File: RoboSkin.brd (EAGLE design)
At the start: 20 x 25.4 mm, 9 parts, among them U1 LSM6DS3, U2 VL53L1X

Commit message: New Circuit
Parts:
- removed L1: RES-07859, SparkFun-Passives:0603
- U1: value LSM6DS3 -> LSM6DS3DOT_INDICATION
- moved U2 66.3 mm to (67.3, 29.2)
- moved R4 57.1 mm to (58.4, 47.0)
- moved R5 57.1 mm to (54.6, 47.0)
- moved SV1 53.9 mm to (53.3, 41.9)
- moved C3 49.3 mm to (50.8, 48.3)
- moved C4 49.3 mm to (47.0, 48.3)
- moved R2 39.7 mm to (44.5, 41.9)
- moved U1 35.0 mm to (36.8, 30.5)
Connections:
- removed net VDD: C3.1, L1.2, U1.8
- net 3.3V: now also C3.1, U1.8; no longer L1.1
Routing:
- net GND: track 50.9 -> 98.8 mm, vias 1 -> 2
- net 3.3V: track 72.6 -> 118.0 mm, vias 2 -> 1
- net SDA: track 16.4 -> 52.8 mm, vias 0 -> 2
- net VDD: track 21.8 -> 0.00 mm, vias 2 -> 0
- net SCL: track 33.0 -> 49.6 mm
- net !SHUT: track 23.7 -> 27.8 mm
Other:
- board size 20 x 25.4 mm -> 100 x 80 mm

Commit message: Kandai Changes in circuit
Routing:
- net SDA: track 52.8 -> 55.8 mm
- net GND: track 98.8 -> 101.0 mm
- net 3.3V: track 118.0 -> 119.1 mm
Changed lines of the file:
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@@
 <contactref element="U1" pad="5"/>
 <contactref element="U1" pad="1"/>
-<wire x1="36.4236" y1="22.0472" x2="36.4236" y2="29.4132" width="0.1524" layer="1"/>
-<wire x1="38.5572" y1="24.1808" x2="36.4236" y2="22.0472" width="0.1524" layer="1"/>
-<wire x1="38.5572" y1="29.4132" x2="38.5572" y2="24.1808" width="0.1524" layer="1"/>
+<wire x1="38.5572" y1="29.4132" x2="38.5572" y2="22.0472" width="0.1524" layer="1"/>
 <wire x1="38.2524" y1="29.718" x2="38.5572" y2="29.4132" width="0.1524" layer="1"/>
 <wire x1="38.1" y1="29.718" x2="38.2524" y2="29.718" width="0.1524" layer="1"/>
-<wire x1="36.4236" y1="29.4132" x2="36.33" y2="29.555" width="0.1524" layer="1"/>
+<wire x1="36.33" y1="29.555" x2="36.4236" y2="29.4132" width="0.1524" layer="1"/>
 <wire x1="38.1" y1="29.718" x2="38.005" y2="29.73" width="0.1524" layer="1"/>
 <wire x1="47.244" y1="41.91" x2="45.3" y2="41.91" width="0.1524" layer="1"/>
@@
 <wire x1="52.1208" y1="41.91" x2="52.07" y2="41.91" width="0.1524" layer="16"/>
 <via x="52.1208" y="47.0916" extent="1-16" drill="0.35"/>
-<wire x1="68.91" y1="30.21" x2="73.39" y2="30.21" width="0.1524" layer="1"/>
+<wire x1="73.39" y1="30.21" x2="68.91" y2="30.21" width="0.1524" layer="1"/>
 <wire x1="68.91" y1="28.21" x2="73.39" y2="28.21" width="0.1524" layer="1"/>
-<wire x1="73.39" y1="28.21" x2="72.39" y2="29.21" width="0.1524" layer="1"/>
-<wire x1="72.39" y1="29.21" x2="73.39" y2="30.21" width="0.1524" layer="1"/>
+<wire x1="36.4236" y1="21.9964" x2="36.83" y2="21.59" width="0.1524" layer="1"/>
+<wire x1="36.83" y1="21.59" x2="38.1" y2="21.59" width="0.1524" layer="1"/>
+<wire x1="38.1" y1="21.59" x2="38.5572" y2="22.0472" width="0.1524" layer="1"/>
+<wire x1="36.4236" y1="29.4132" x2="36.4236" y2="21.9964" width="0.1524" layer="1"/>
+<wire x1="73.39" y1="28.21" x2="73.66" y2="28.48" width="0.1524" layer="1"/>
+<wire x1="73.66" y1="29.94" x2="73.39" y2="30.21" width="0.1524" layer="1"/>
+<wire x1="73.66" y1="28.48" x2="73.66" y2="29.94" width="0.1524" layer="1"/>
 </signal>
 <signal name="SCL">
@@
 <contactref element="U1" pad="14"/>
 <contactref element="SV1" pad="3"/>
-<wire x1="36.4236" y1="31.6992" x2="36.4236" y2="31.5468" width="0.1524" layer="1"/>
-<wire x1="42.0624" y1="37.338" x2="36.4236" y2="31.6992" width="0.1524" layer="1"/>
+<wire x1="36.4236" y1="36.7792" x2="36.4236" y2="31.5468" width="0.1524" layer="1"/>
+<wire x1="42.0624" y1="37.338" x2="36.9824" y2="37.338" width="0.1524" layer="1"/>
+<wire x1="36.9824" y1="37.338" x2="36.4236" y2="36.7792" width="0.1524" layer="1"/>
 <wire x1="42.672" y1="37.338" x2="42.0624" y2="37.338" width="0.1524" layer="16"/>
 <wire x1="49.0728" y1="43.7388" x2="42.672" y2="37.338" width="0.1524" layer="16"/>
@@
 <wire x1="31.5468" y1="30.3276" x2="35.3568" y2="30.3276" width="0.1524" layer="1"/>
 <wire x1="35.3568" y1="30.3276" x2="35.5092" y2="30.3276" width="0.1524" layer="1"/>
+<wire x1="32.3596" y1="33.3248" x2="35.2044" y2="30.48" width="0.1524" layer="1"/>
 <wire x1="35.2044" y1="30.48" x2="35.3568" y2="30.3276" width="0.1524" layer="1"/>
-<wire x1="35.5092" y1="30.7848" x2="35.3568" y2="30.6324" width="0.1524" layer="1"/>
-<wire x1="35.3568" y1="30.6324" x2="35.2044" y2="30.48" width="0.1524" layer="1"/>
+<wire x1="35.5092" y1="30.7848" x2="35.2044" y2="30.48" width="0.1524" layer="1"/>
 <wire x1="35.5092" y1="30.3276" x2="35.655" y2="30.23" width="0.1524" layer="1"/>
 <wire x1="35.5092" y1="30.7848" x2="35.655" y2="30.73" width="0.1524" layer="1"/>
@@
 <wire x1="46.9392" y1="49.0728" x2="47.7012" y2="48.3108" width="0.1524" layer="1"/>
 <wire x1="45.5676" y1="49.0728" x2="46.9392" y2="49.0728" width="0.1524" layer="1"/>
-<wire x1="34.8996" y1="38.4048" x2="45.5676" y2="49.0728" width="0.1524" layer="1"/>
-<wire x1="34.8996" y1="31.0896" x2="34.8996" y2="38.4048" width="0.1524" layer="1"/>
-<wire x1="35.3568" y1="30.6324" x2="34.8996" y2="31.0896" width="0.1524" layer="1"/>
+<wire x1="32.3596" y1="35.8648" x2="45.5676" y2="49.0728" width="0.1524" layer="1"/>
+<wire x1="32.3596" y1="33.3248" x2="32.3596" y2="35.8648" width="0.1524" layer="1"/>
 <wire x1="47.7012" y1="48.3108" x2="47.84" y2="48.26" width="0.1524" layer="1"/>
 <wire x1="62.1792" y1="29.2608" x2="65.2272" y2="29.2608" width="0.1524" layer="1"/>

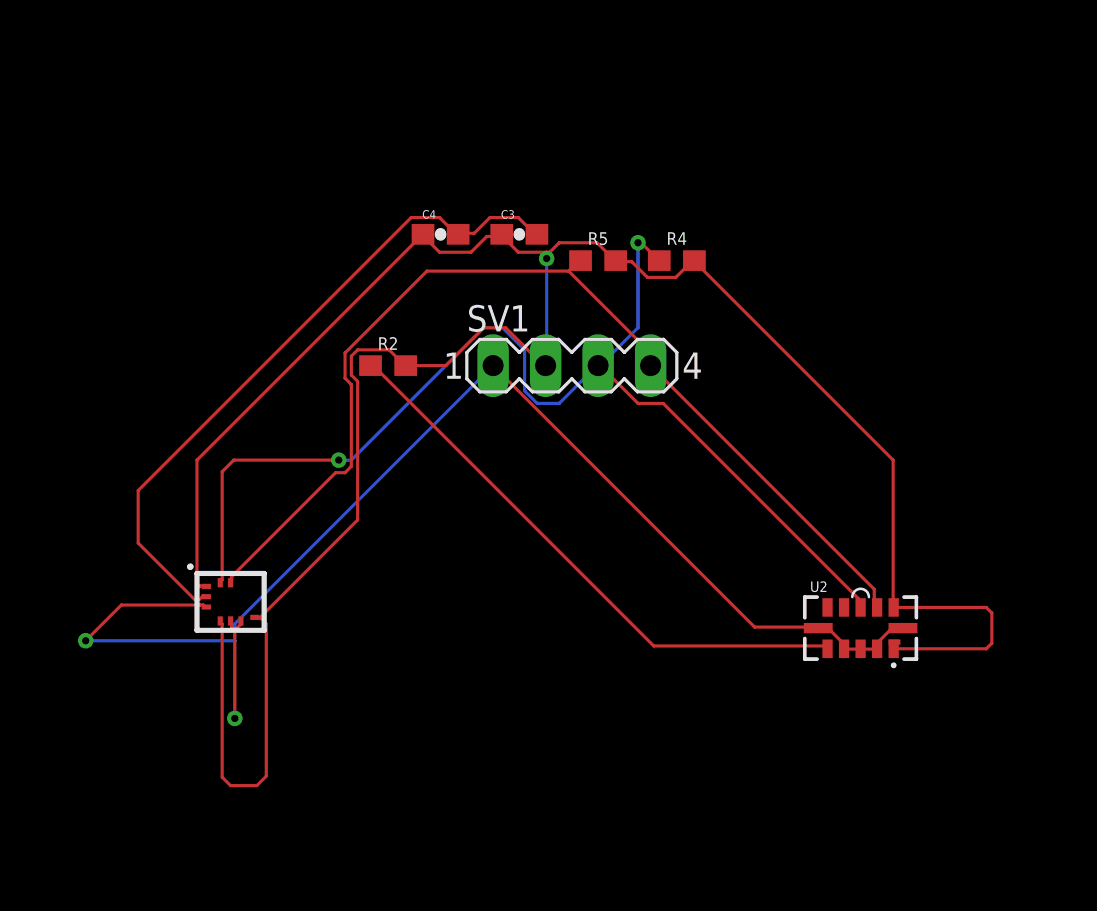
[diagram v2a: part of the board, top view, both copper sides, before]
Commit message: Increased spacing
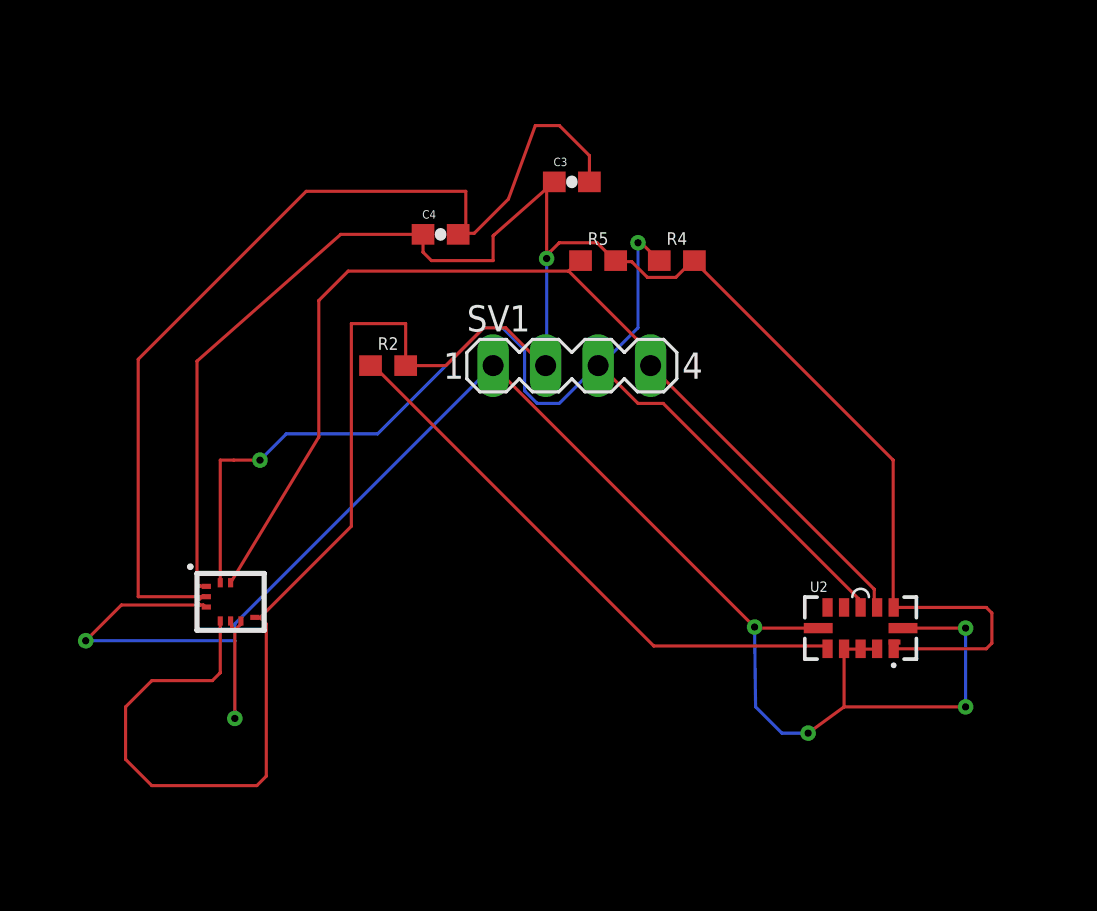
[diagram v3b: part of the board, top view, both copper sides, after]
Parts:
- moved C3 3.59 mm to (53.3, 50.8)
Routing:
- net GND: track 101.0 -> 137.5 mm, vias 2 -> 6
- net 3.3V: track 119.1 -> 138.8 mm
- net SCL: track 49.6 -> 50.9 mm

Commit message: Kandai Changes
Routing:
- net 3.3V: track 138.8 -> 128.2 mm
- net GND: track 137.5 -> 147.5 mm, vias 6 -> 5

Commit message: New Skin Circuit
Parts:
- moved U2 18.3 mm to (57.1, 44.5)
- moved U1 18.1 mm to (48.3, 44.5)
- moved SV1 13.1 mm to (64.8, 48.3), turned to 270 degrees
- moved C4 11.4 mm to (57.1, 53.3)
- moved R2 9.16 mm to (49.5, 49.5)
- moved C3 8.03 mm to (61.0, 53.3)
- moved R4 2.84 mm to (59.7, 49.5)
- moved R5 2.54 mm to (54.6, 49.5)
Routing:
- net GND: track 147.5 -> 57.3 mm, vias 5 -> 2
- net 3.3V: track 128.2 -> 70.2 mm
- net SDA: track 56.4 -> 34.2 mm
- net SCL: track 51.1 -> 41.8 mm, vias 0 -> 2
- net !SHUT: track 27.8 -> 24.4 mm

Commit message: Push Latest Changes to Git
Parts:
- moved C4 15.5 mm to (41.9, 55.9)
- moved C3 13.0 mm to (48.3, 55.9)
- moved U1 8.98 mm to (41.9, 38.1)
- moved R4 8.13 mm to (64.8, 55.9)
- moved R2 7.73 mm to (41.9, 48.3)
- moved R5 6.48 mm to (55.9, 55.9)
- moved U2 4.58 mm to (53.3, 47.0)
- moved SV1 2.54 mm to (64.8, 45.7), turned to 90 degrees
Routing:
- net 3.3V: track 70.2 -> 132.5 mm, vias 1 -> 3
- net GND: track 57.3 -> 114.3 mm, vias 2 -> 3
- net SDA: track 34.2 -> 72.1 mm, vias 2 -> 1
- net !SHUT: track 24.4 -> 16.2 mm
- net SCL: track 41.8 -> 49.5 mm, vias 2 -> 1

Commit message: fixed wiring
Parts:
- moved C3 1.27 mm to (47.0, 55.9)
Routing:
- net GND: track 114.3 -> 109.1 mm
- net !SHUT: track 16.2 -> 14.1 mm
- net 3.3V: track 132.5 -> 133.5 mm

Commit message: Small Update in schematics
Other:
- board size 100 x 80 mm -> 36.5 x 26.7 mm
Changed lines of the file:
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@@
 <board>
 <plain>
-<wire x1="0" y1="0" x2="100" y2="0" width="0" layer="20"/>
-<wire x1="100" y1="0" x2="100" y2="80" width="0" layer="20"/>
-<wire x1="100" y1="80" x2="0" y2="80" width="0" layer="20"/>
-<wire x1="0" y1="80" x2="0" y2="0" width="0" layer="20"/>
+<wire x1="34.29" y1="33.02" x2="70.79" y2="33.02" width="0" layer="20"/>
+<wire x1="70.79" y1="33.02" x2="70.79" y2="59.68" width="0" layer="20"/>
+<wire x1="70.79" y1="59.68" x2="34.29" y2="59.68" width="0" layer="20"/>
+<wire x1="34.29" y1="59.68" x2="34.29" y2="33.02" width="0" layer="20"/>
 </plain>
 <attributes>
@@
 <classes>
 <class number="0" name="default" width="0" drill="0">
+<clearance class="0" value="0.205"/>
 </class>
 </classes>
